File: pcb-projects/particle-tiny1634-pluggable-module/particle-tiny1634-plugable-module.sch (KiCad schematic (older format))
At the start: 33 parts, among them IC1 ATTINY1634-SU, P1 INTERFACE, P2 MCU_TEST

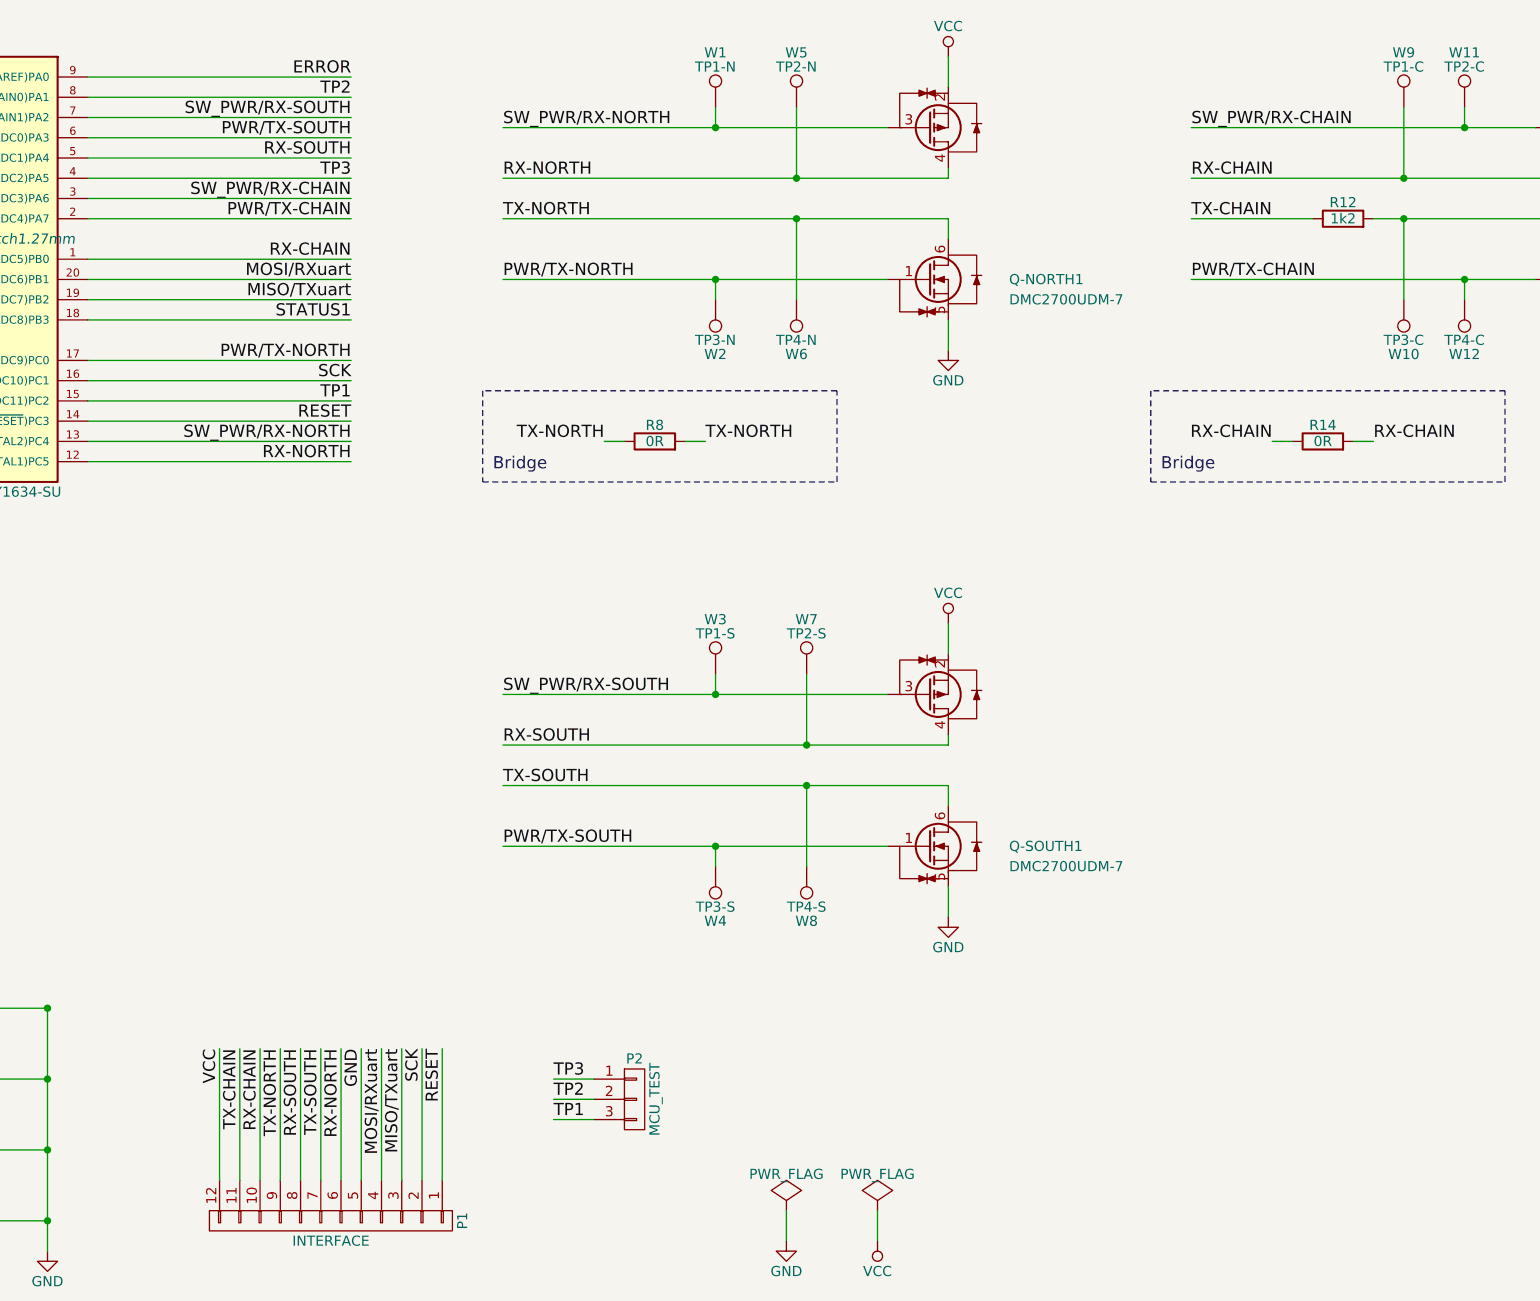
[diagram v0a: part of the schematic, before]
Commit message: changed network names slightly
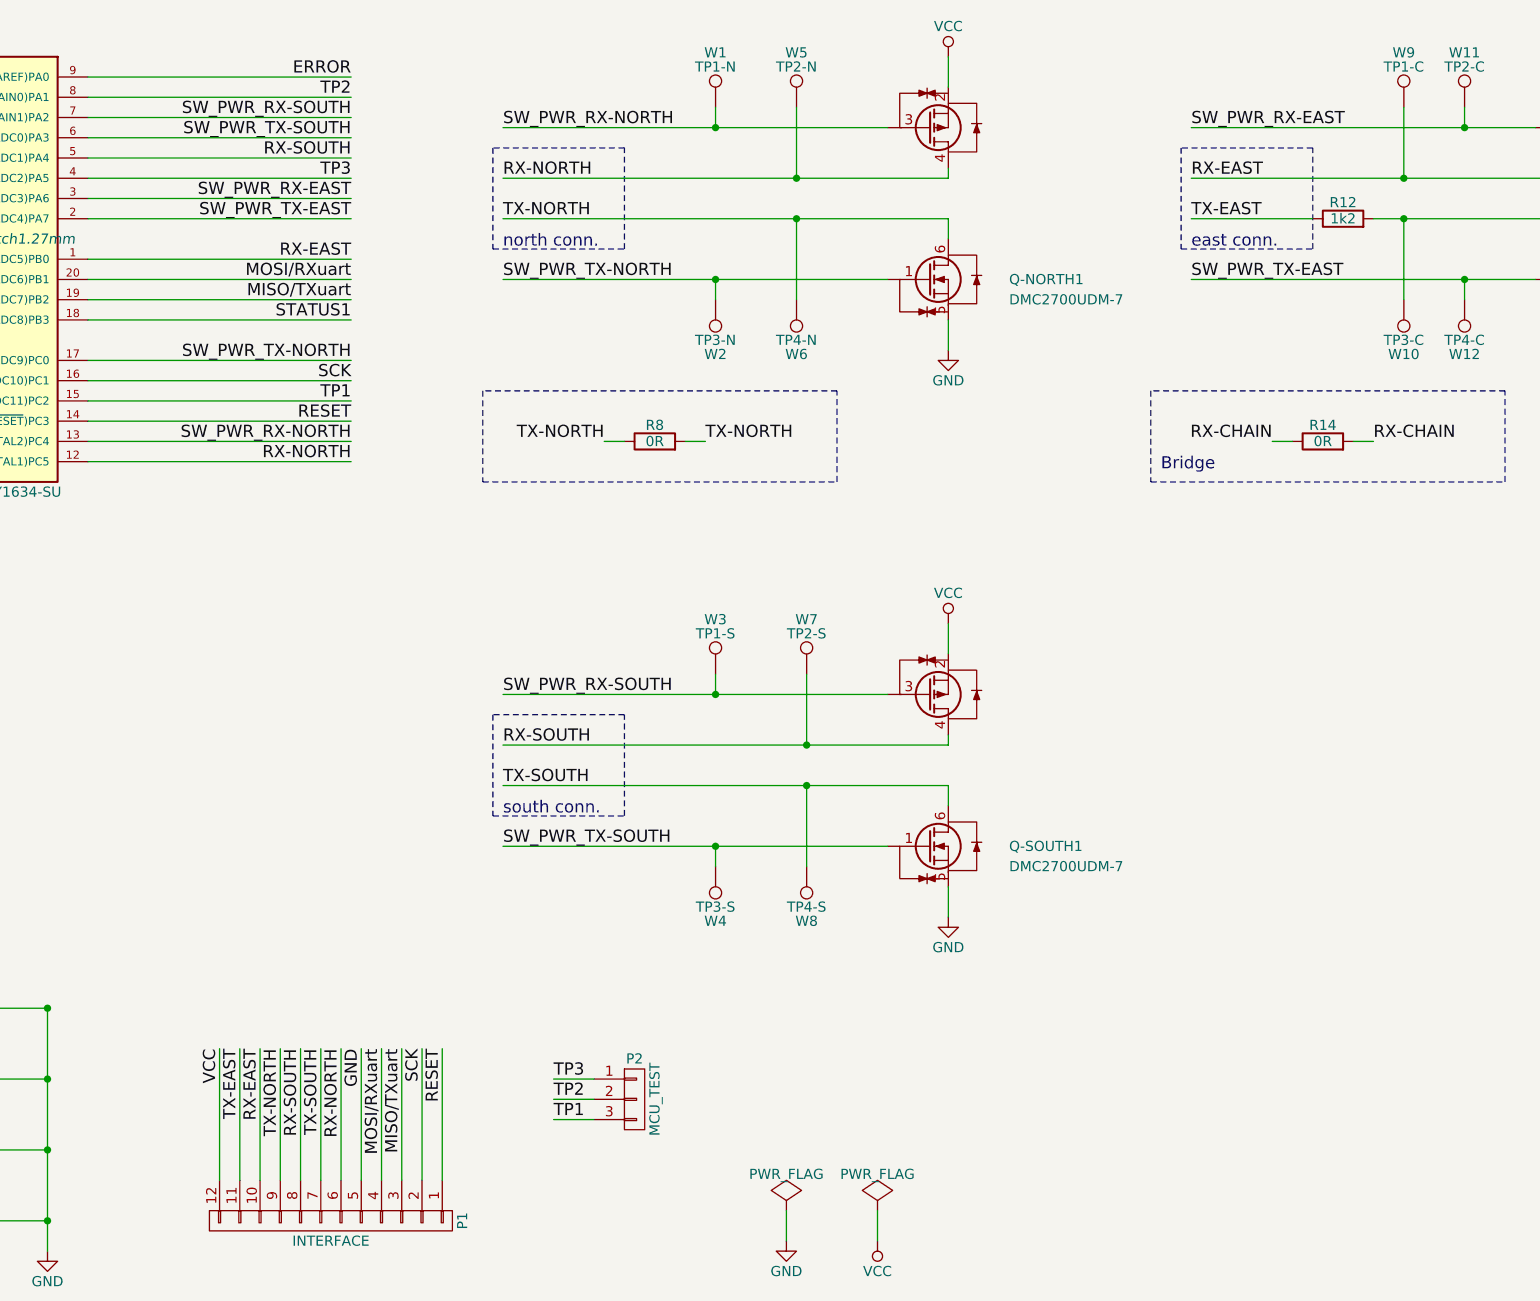
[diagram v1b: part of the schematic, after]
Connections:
- net RX-CHAIN: no longer IC1.1 ((PCINT8/TXD0/ADC5)PB0), P1.10 (P10), Q-CHAIN1.4 (D2), W9.1
- net PWR/TX-CHAIN renamed SW_PWR_TX-EAST
- net PWR/TX-NORTH renamed SW_PWR_TX-NORTH
- net PWR/TX-SOUTH renamed SW_PWR_TX-SOUTH
- net SW_PWR/RX-CHAIN renamed SW_PWR_RX-EAST
- net SW_PWR/RX-NORTH renamed SW_PWR_RX-NORTH
- net SW_PWR/RX-SOUTH renamed SW_PWR_RX-SOUTH
- net TX-CHAIN renamed TX-EAST
- new net RX-EAST: IC1.1 ((PCINT8/TXD0/ADC5)PB0), P1.10 (P10), Q-CHAIN1.4 (D2), W9.1
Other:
- note added: "east conn."
- note added: "north conn."
- note added: "south conn."

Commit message: cleanup folders; minimal pcb changes
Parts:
- renumbered Q-CHAIN1 to Q-EAST1
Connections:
- net RX-CHAIN is gone; now on net RX-EAST: R14.1, R14.2
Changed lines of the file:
@@
 TX-SOUTH
 $Comp
-L DMC2700UDM-7 Q-CHAIN1
+L DMC2700UDM-7 Q-EAST1
 U 1 1 56A8C6DF
 P 10150 2700
-F 0 "Q-CHAIN1" H 10550 2700 50  0000 L CNN
+F 0 "Q-EAST1" H 10550 2700 50  0000 L CNN
 F 1 "DMC2700UDM-7" H 10550 2600 50  0000 L CNN
 F 2 "sot26:SOT-26" H 10320 2580 50  0001 C CNN
@@
 $EndComp
 Text Label 9150 3500 0    60   ~ 0
-RX-CHAIN
+RX-EAST
 Text Label 8650 3500 2    60   ~ 0
-RX-CHAIN
+RX-EAST
 $Comp
 L VCC #PWR016
